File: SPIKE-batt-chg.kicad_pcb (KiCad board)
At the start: 2 copper layers, 109 parts, among them IC1 CN3702, IC2 CH224K, IC3 CN3702, IC4 CN3702, J1 USB_C_Receptacle_USB2.0, J2 Barrel_Jack_Switch, J3 Conn_01x03_Pin, J4 Conn_01x03_Pin, J5 Conn_01x03_Pin, Q1 PMOS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

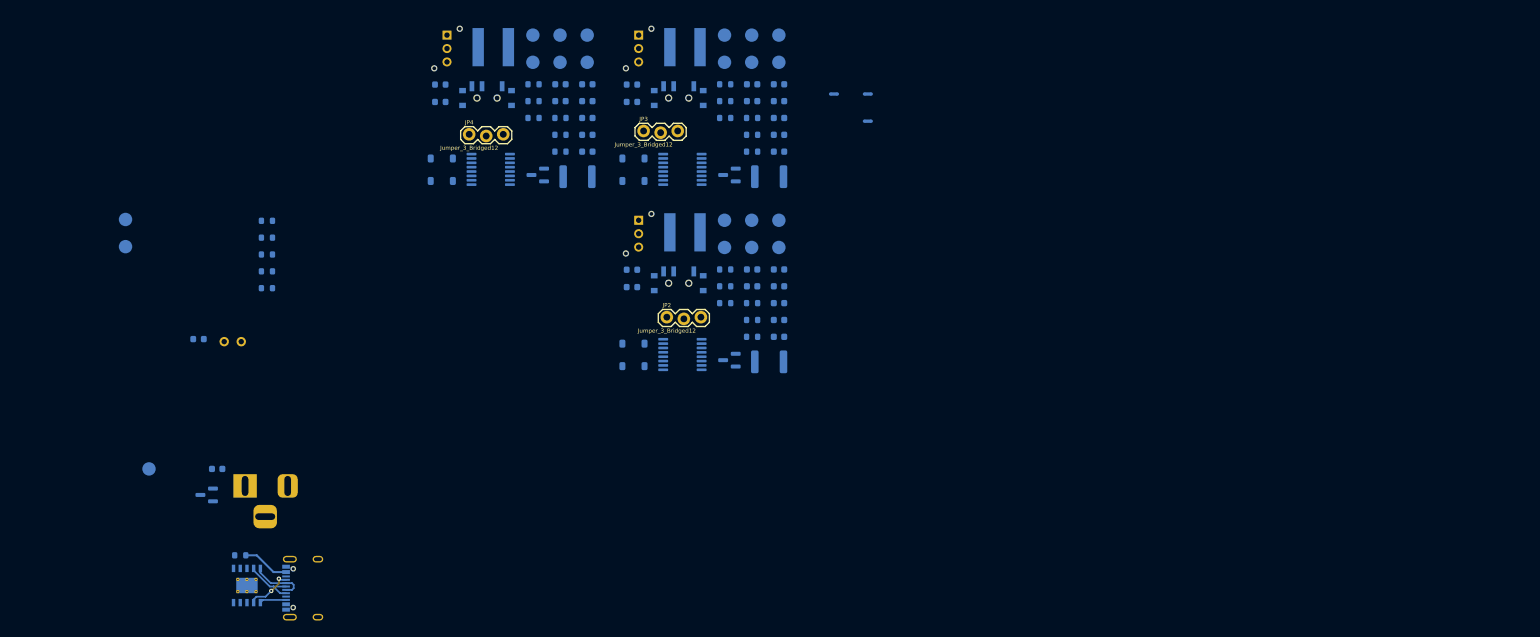
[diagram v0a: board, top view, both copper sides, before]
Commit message: CH224K Board Layout complete
- Partial layout of CN3702
- Fixed the incorrect NetTie on 2sLipoCharger.kicad_sch (More things are supposed to go to AGND)
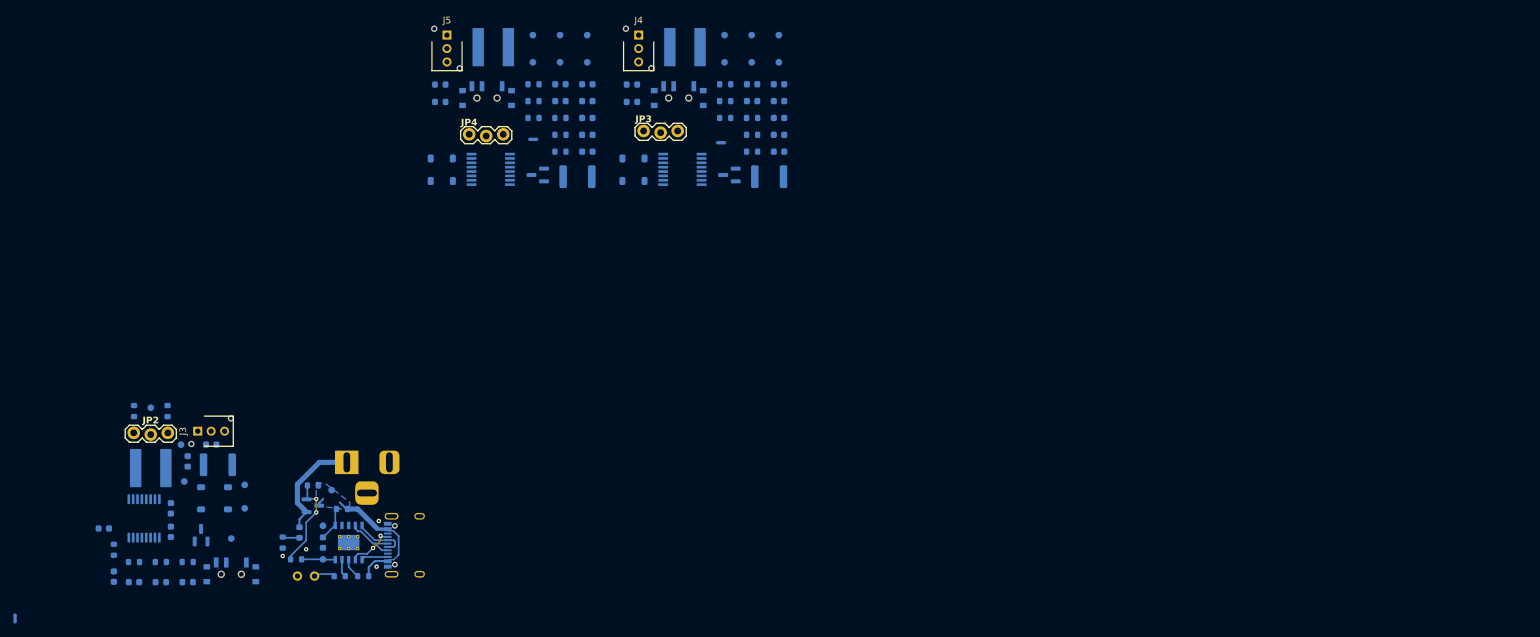
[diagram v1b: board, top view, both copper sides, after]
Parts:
- J3, J4, J5: moved to F.Cu
- TP1, TP10, TP11, TP12, TP13, TP14, TP15, TP16, TP17, TP18, TP19, TP2, TP20, TP21, TP3, TP4, TP5, TP6, TP7, TP8, TP9: footprint TestPoint:TestPoint_Pad_D2.0mm -> TestPoint:TestPoint_Pad_D1.0mm
- moved NT1 147.1 mm to (41.8, 156.9), turned to -90 degrees
- moved C5 106.3 mm to (56.5, 150.7), turned to -90 degrees
- moved C4 104.8 mm to (59.5, 151.5), turned to 0 degrees
- moved C6 104.6 mm to (55.0, 143.5)
- moved R10 100.2 mm to (56.5, 146.7), turned to -90 degrees
- moved R9 98.1 mm to (59.5, 148.5), turned to 0 degrees
- moved C3 97.8 mm to (65.0, 144.0), turned to -90 degrees
- moved TP4 97.7 mm to (62.0, 125.5)
- moved C2 97.4 mm to (65.0, 140.5), turned to -90 degrees
- moved R7 96.2 mm to (63.5, 148.5)
- moved TP5 95.2 mm to (67.0, 136.5)
- moved R8 91.5 mm to (67.5, 148.5)
- moved R11 90.1 mm to (59.5, 126.0), turned to 90 degrees
- moved C7 88.9 mm to (67.5, 133.5), turned to 90 degrees
- moved TP8 87.7 mm to (66.5, 131.0)
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- renumbered IC2 to IC1, IC1 to IC2
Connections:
- C11 pad 2: GND -> GNDA
- C12 pad 2: GND -> GNDA
- C13 pad 2: GND -> GNDA
- C18 pad 2: GND -> GNDA
- C19 pad 2: GND -> GNDA
- C20 pad 2: GND -> GNDA
- C4 pad 2: GND -> GNDA
- C5 pad 2: GND -> GNDA
- C6 pad 2: GND -> GNDA
- IC2 pad 10: GND -> GNDA
- IC2 pad 3: Net-(IC1-GND) -> GNDA
- IC3 pad 10: GND -> GNDA
- IC3 pad 3: Net-(IC3-GND) -> GNDA
- IC4 pad 10: GND -> GNDA
- IC4 pad 3: Net-(IC4-GND) -> GNDA
- NT1 pad 2: Net-(IC1-GND) -> GNDA
- NT2 pad 2: Net-(IC3-GND) -> GNDA
- NT3 pad 2: Net-(IC4-GND) -> GNDA
- R15 pad 2: GND -> GNDA
- R21 pad 2: GND -> GNDA
- R9 pad 2: GND -> GNDA
- SW1 pad 1: GND -> GNDA
- SW2 pad 1: GND -> GNDA
- SW3 pad 1: GND -> GNDA
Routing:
- net VCC: track 0.00 -> 16.1 mm
- net VBUS: track 7.08 -> 21.4 mm
- net Net-(Q1-G): track 0.00 -> 14.1 mm, vias 0 -> 2
- net VDD: track 0.00 -> 5.09 mm
- net Net-(IC1-PG): track 0.00 -> 5.03 mm
- net Net-(JP1-B): track 0.00 -> 3.06 mm
- net Net-(IC1-VBUS): track 0.00 -> 3.00 mm
- net Net-(IC1-CFG1): track 0.00 -> 2.65 mm
- net Net-(D1-K): track 0.00 -> 2.55 mm
- net GND: vias 0 -> 4
- added copper zone on B.Cu, net VBUS

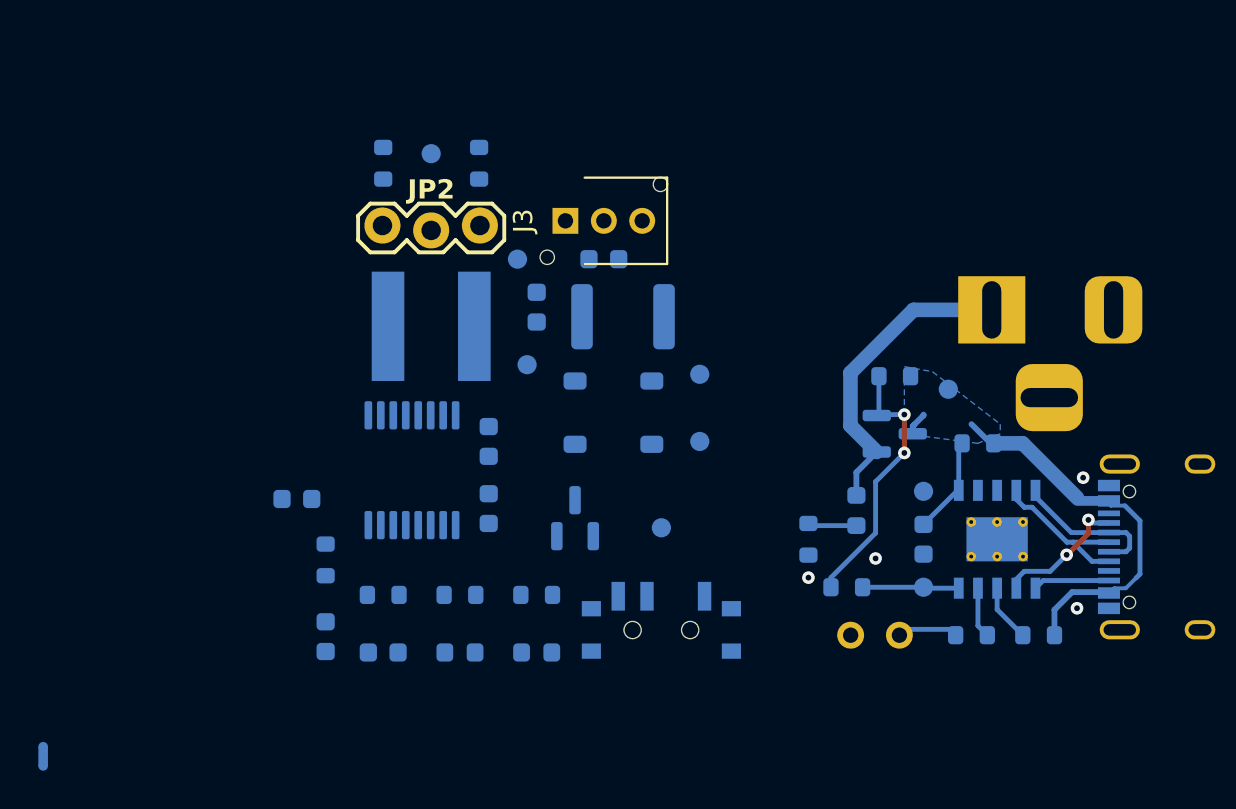
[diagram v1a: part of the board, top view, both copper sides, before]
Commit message: Finished charger layout
- Replace global power symbols in charger schematic with local labels
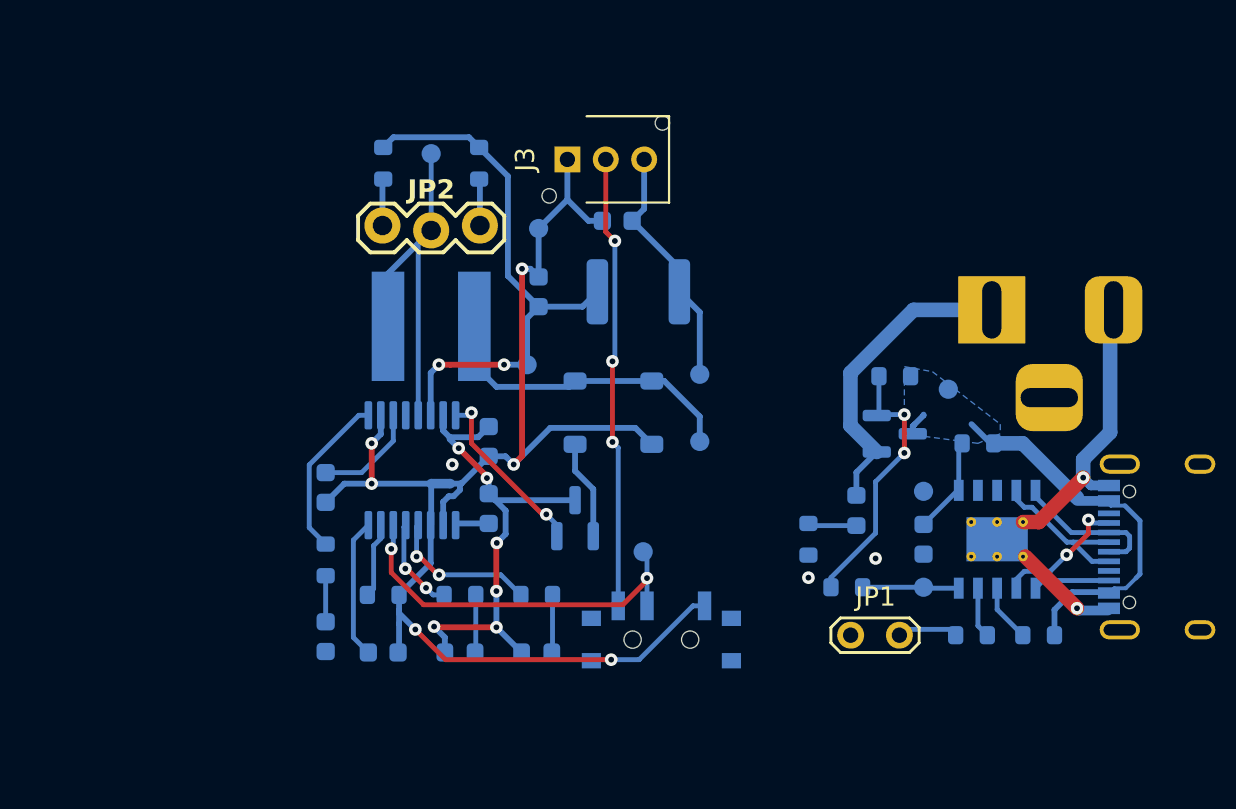
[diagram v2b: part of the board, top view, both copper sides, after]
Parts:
- JP1: moved to F.Cu
- moved NT1 25.1 mm to (62.5, 142.7), turned to 180 degrees
- moved J3 3.20 mm to (69.1, 125.8)
- moved C8 2.12 mm to (71.7, 129.0)
- moved TP8 1.94 mm to (67.6, 129.4)
- moved C6 1.62 mm to (56.5, 142.9), turned to -90 degrees
- moved TP9 1.57 mm to (73.0, 146.2)
- moved F1 1.53 mm to (72.8, 132.7)
- moved C7 0.81 mm to (67.6, 132.7)
- moved SW1 0.50 mm to (74.0, 150.5)
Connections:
- C11 pad 2: GNDA -> /CN3702 Charger2/GNDA
- C12 pad 2: GNDA -> /CN3702 Charger2/GNDA
- C13 pad 2: GNDA -> /CN3702 Charger2/GNDA
- C15 pad 1: +BATT -> /CN3702 Charger2/+BATT
- C18 pad 2: GNDA -> /CN3702 Charger3/GNDA
- C19 pad 2: GNDA -> /CN3702 Charger3/GNDA
- C20 pad 2: GNDA -> /CN3702 Charger3/GNDA
- C22 pad 1: +BATT -> /CN3702 Charger3/+BATT
- C4 pad 2: GNDA -> /CN3702 Charger1/GNDA
- C5 pad 2: GNDA -> /CN3702 Charger1/GNDA
- C6 pad 2: GNDA -> /CN3702 Charger1/GNDA
- C8 pad 1: +BATT -> /CN3702 Charger1/+BATT
- F1 pad 2: +BATT -> /CN3702 Charger1/+BATT
- F2 pad 2: +BATT -> /CN3702 Charger2/+BATT
- F3 pad 2: +BATT -> /CN3702 Charger3/+BATT
- IC2 pad 10: GNDA -> /CN3702 Charger1/GNDA
- IC2 pad 3: GNDA -> /CN3702 Charger1/GNDA
- IC3 pad 10: GNDA -> /CN3702 Charger2/GNDA
- IC3 pad 3: GNDA -> /CN3702 Charger2/GNDA
- IC4 pad 10: GNDA -> /CN3702 Charger3/GNDA
- IC4 pad 3: GNDA -> /CN3702 Charger3/GNDA
- J3 pad 3: +BATT -> /CN3702 Charger1/+BATT
- J4 pad 3: +BATT -> /CN3702 Charger2/+BATT
- J5 pad 3: +BATT -> /CN3702 Charger3/+BATT
- NT1 pad 2: GNDA -> /CN3702 Charger1/GNDA
- NT2 pad 2: GNDA -> /CN3702 Charger2/GNDA
- NT3 pad 2: GNDA -> /CN3702 Charger3/GNDA
- R15 pad 2: GNDA -> /CN3702 Charger2/GNDA
- R21 pad 2: GNDA -> /CN3702 Charger3/GNDA
- R9 pad 2: GNDA -> /CN3702 Charger1/GNDA
- SW1 pad 1: GNDA -> /CN3702 Charger1/GNDA
- SW2 pad 1: GNDA -> /CN3702 Charger2/GNDA
- SW3 pad 1: GNDA -> /CN3702 Charger3/GNDA
- TP10 pad 1: +BATT -> /CN3702 Charger2/+BATT
- TP16 pad 1: +BATT -> /CN3702 Charger3/+BATT
- TP7 pad 1: +BATT -> /CN3702 Charger1/+BATT
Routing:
- net GND: track 0.00 -> 56.1 mm, vias 4 -> 7
- net /CN3702 Charger1/GNDA: track 0.00 -> 37.4 mm, vias 0 -> 4
- net /CN3702 Charger1/BAT: track 0.00 -> 29.1 mm, vias 0 -> 2
- net VCC: track 16.1 -> 42.4 mm, vias 0 -> 6
- net /CN3702 Charger1/NTC: track 0.00 -> 23.6 mm, vias 0 -> 3
- net /CN3702 Charger1/TEMP: track 0.00 -> 20.1 mm, vias 0 -> 2
- net /CN3702 Charger1/CSP: track 0.00 -> 18.9 mm
- net Net-(D4-K): track 0.00 -> 16.4 mm
- net /CN3702 Charger1/+BATT: track 0.00 -> 12.9 mm
- net Net-(IC2-DRV): track 0.00 -> 9.28 mm, vias 0 -> 2
- net Net-(IC2-COM2): track 0.00 -> 8.63 mm
- net Net-(IC2-CHRG): track 0.00 -> 7.94 mm, vias 0 -> 2
- net Net-(IC2-COM1): track 0.00 -> 7.28 mm
- net Net-(IC2-COM3): track 0.00 -> 5.55 mm
- net Net-(D4-A): track 0.00 -> 5.18 mm
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
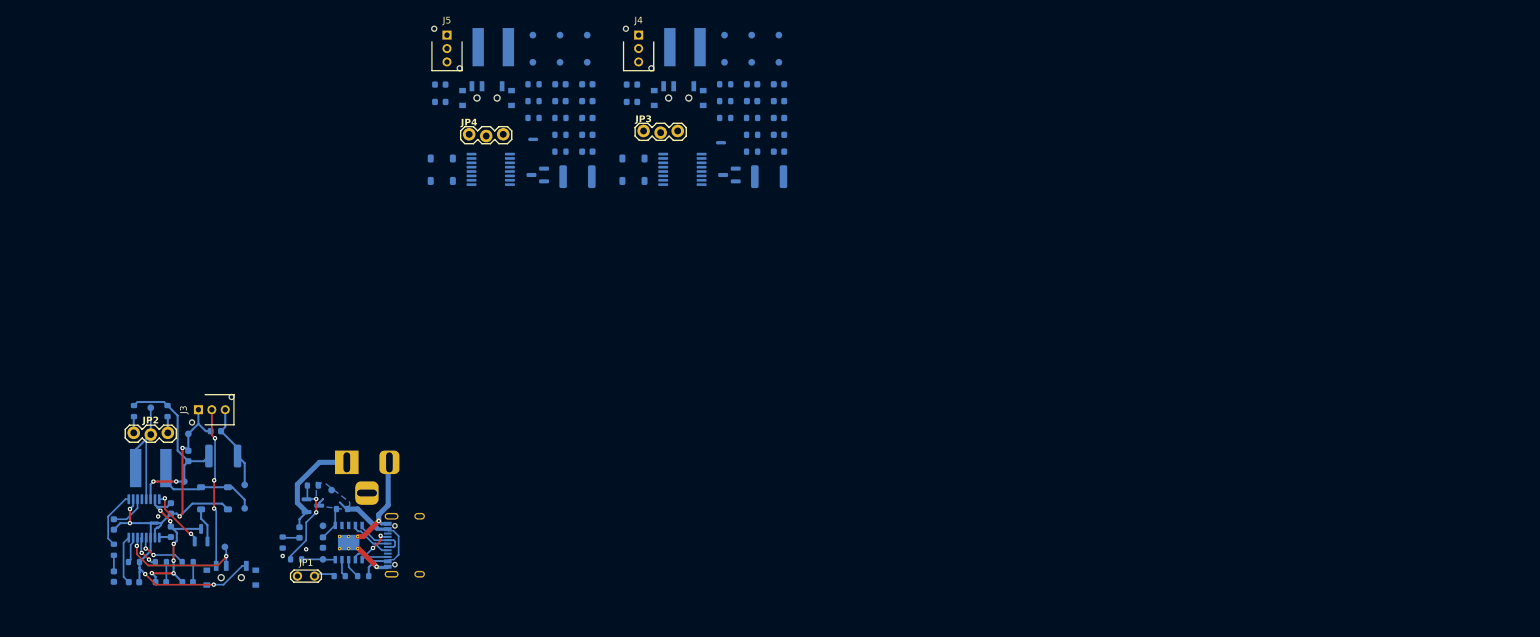
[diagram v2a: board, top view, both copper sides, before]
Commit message: Finished layout
- DRC checked, outline complete
- Left to do: silkscreen
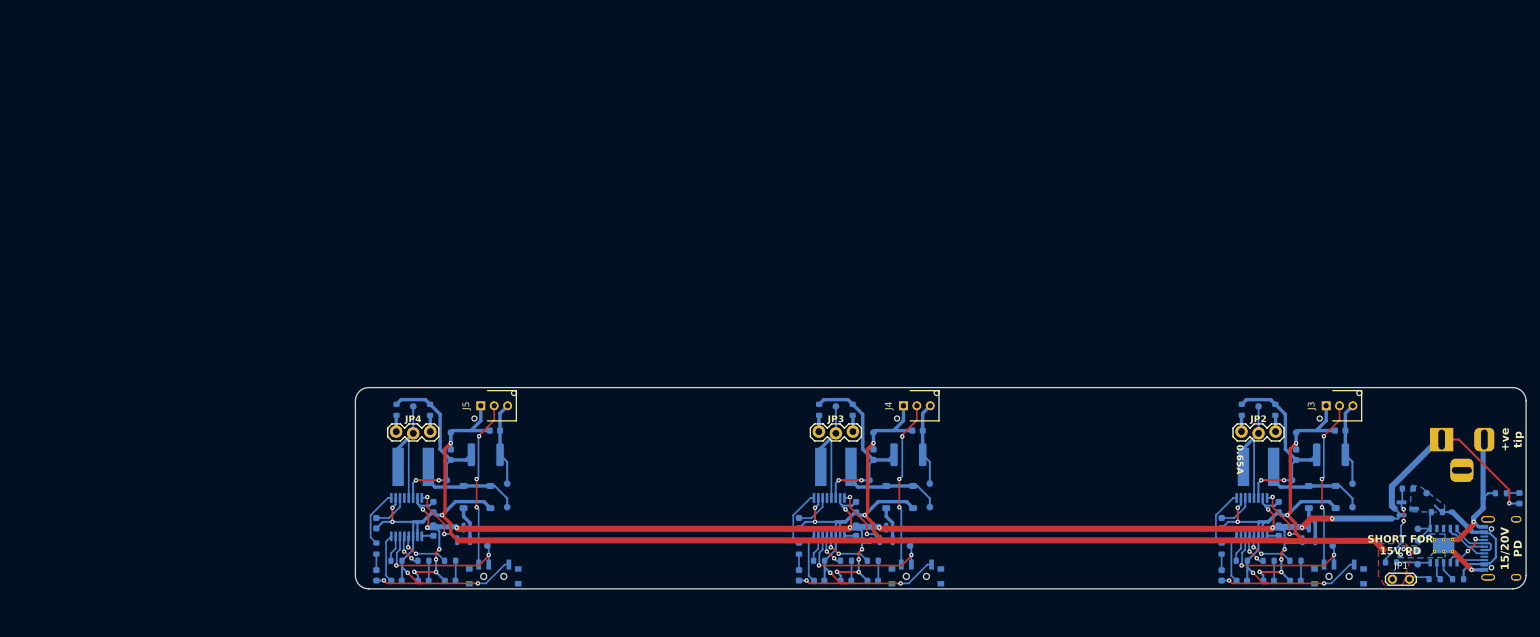
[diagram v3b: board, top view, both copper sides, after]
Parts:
- moved D1 181.9 mm to (266.0, 139.0), turned to -90 degrees
- moved R4 181.7 mm to (263.2, 138.2), turned to 180 degrees
- moved J3 168.1 mm to (237.2, 125.2)
- moved C8 167.6 mm to (239.3, 128.9)
- moved C2 165.1 mm to (230.1, 140.3)
- moved C3 165.1 mm to (230.1, 143.8)
- moved C4 165.1 mm to (224.6, 151.3)
- moved C5 165.1 mm to (221.6, 150.5)
- moved C6 165.1 mm to (221.6, 142.7)
- moved C7 165.1 mm to (232.7, 132.5)
- moved D2 165.1 mm to (228.6, 151.3)
- moved D3 165.1 mm to (232.6, 151.3)
- moved D4 165.1 mm to (234.6, 138.8)
- moved D5 165.1 mm to (238.6, 138.8)
- moved F1 165.1 mm to (237.9, 132.5)
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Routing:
- net GND: track 56.1 -> 325.4 mm, vias 7 -> 11
- net VCC: track 42.4 -> 247.9 mm, vias 6 -> 23
- net /CN3702 Charger2/GNDA: track 0.00 -> 44.6 mm, vias 0 -> 5
- net /CN3702 Charger3/GNDA: track 0.00 -> 44.3 mm, vias 0 -> 5
- net /CN3702 Charger3/BAT: track 0.00 -> 29.2 mm, vias 0 -> 2
- net /CN3702 Charger2/BAT: track 0.00 -> 29.2 mm, vias 0 -> 2
- net /CN3702 Charger2/NTC: track 0.00 -> 24.9 mm, vias 0 -> 3
- net /CN3702 Charger3/NTC: track 0.00 -> 24.9 mm, vias 0 -> 3
- net /CN3702 Charger2/TEMP: track 0.00 -> 22.0 mm, vias 0 -> 2
- net /CN3702 Charger3/TEMP: track 0.00 -> 22.0 mm, vias 0 -> 2
- net /CN3702 Charger3/+BATT: track 0.00 -> 20.3 mm
- net /CN3702 Charger2/+BATT: track 0.00 -> 20.3 mm
- net /CN3702 Charger2/CSP: track 0.00 -> 18.9 mm
- net /CN3702 Charger3/CSP: track 0.00 -> 18.9 mm
- net Net-(D8-K): track 0.00 -> 16.3 mm
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- added copper zone on B.Cu, net GND
- added copper zone on F.Cu, net GND
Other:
- board outline added: 174.5 x 30 mm
- board text added: "+ve tip"
- board text added: "0.65A"
- board text added: "15/20V PD"
- board text added: "SHORT FOR 15V PD"
